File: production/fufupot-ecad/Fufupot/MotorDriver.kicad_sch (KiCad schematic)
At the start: 0 parts

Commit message: Added on to MCU outputs and added motor controller outputs
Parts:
- added 16MHz1: Crystal, 16 MHz Xtal Osc:XTAL_ABL-16_ABR, symbol Device:Crystal
- added C1, C2: 22pF, 22 pF Cap:CAP_K-SERIES_15-L2_VIS, symbol Device:C
- added C3: 10uF, 10 uF Cap:CAP_YX_5X11_RUB, symbol Device:C_Polarized
- added C5: 0.1 uF, 0.1 uF:CAP_Y5VE5TL2_VIS, symbol Device:C
- added J1: PPTC061LFBN-RC, 6 Pin:CONN6_061LFBN-RC_SUL, symbol 6 PIN Header:PPTC061LFBN-RC
- added R1: 10k, 10K Ohm:CAP_YX_5X11_RUB, symbol Device:R
- added U1: 282837-3, Screw Term 3 pin:282837-3_TYC, symbol 3 Pin Screw Term:282837-3
- added U2: ATMEGA328P-PN, footprints:28P3_ATM, symbol 2023-10-12_03-24-27:ATMEGA328P-PN
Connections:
- new net: 16MHz1.1, C2.2, U2.10 (PB7)
- new net: 16MHz1.2, C1.2, U2.9 (PB6)
- new net: C5.1, J1.1
- new net +48V: U1.3
- new net +5V: C3.1, J1.5, R1.1, U1.2, U2.20 (AVCC)
- new net CAT Heat: U2.23 (PC0)
- new net GND: C1.1, C2.1, C3.2, J1.6, U1.1, U2.7 (VCC), U2.8 (GND)
- new net PWM Speed Control: U2.15 (PB1)
- new net RESET: C5.2, R1.2, U2.1 (PC6)
- new net RX: J1.3, U2.2 (PD0)
- new net TX: J1.2, U2.3 (PD1)
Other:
- note added: "Motor Driver PCB Screw Terminal"
- note added: "This connects to the 0-5V terminal on the motor controller"

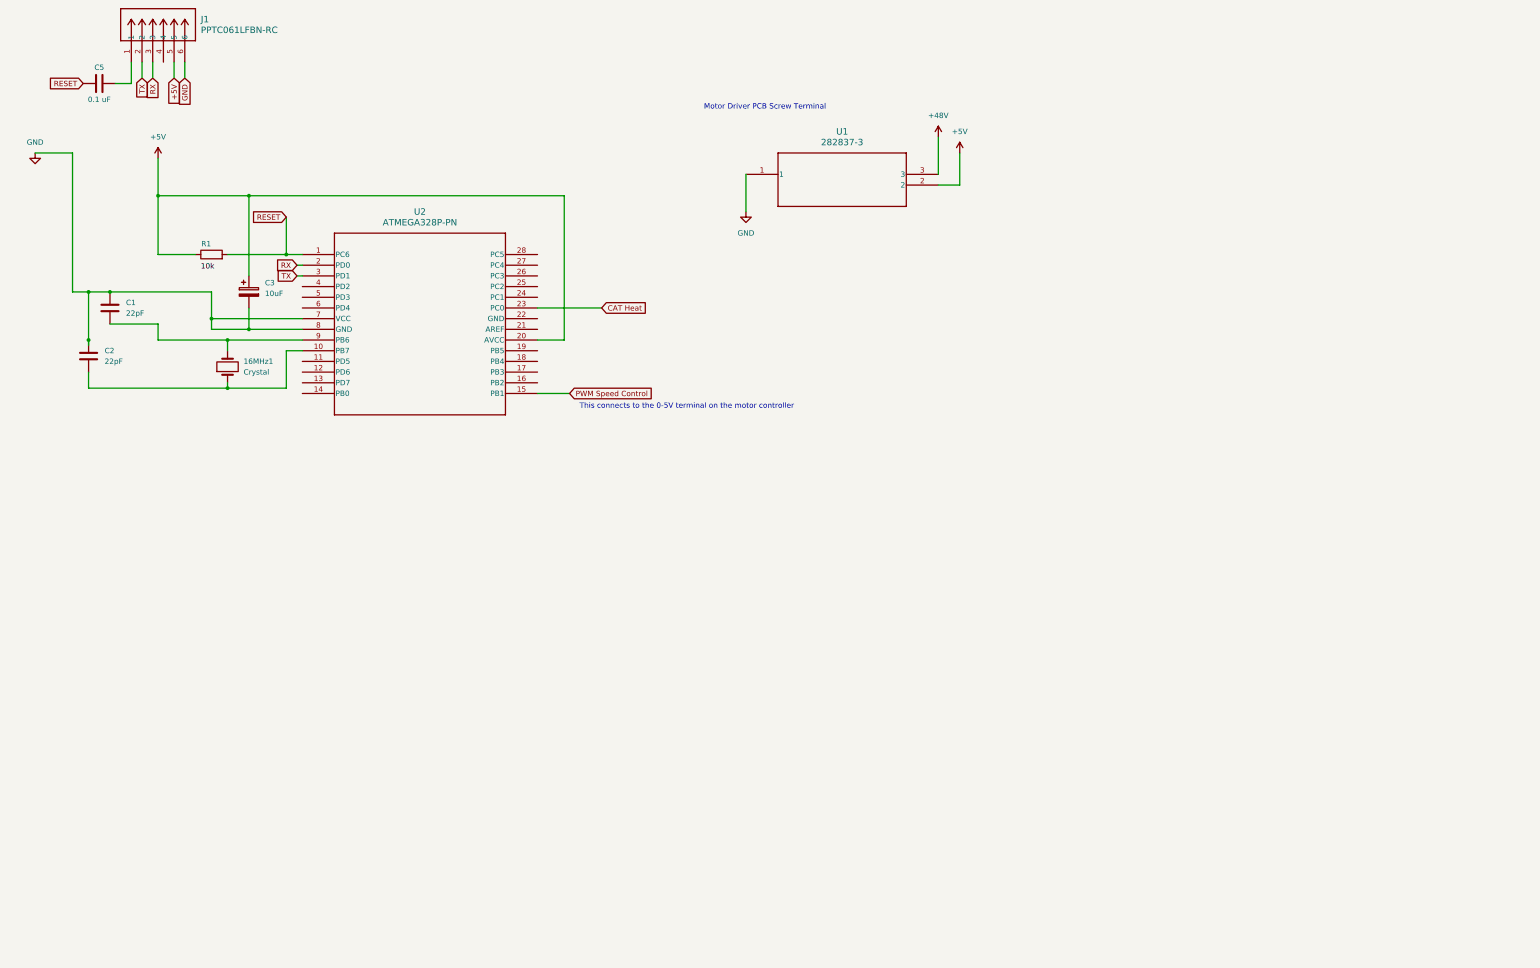
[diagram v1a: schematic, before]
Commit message: Andy's Updates
Updating from Andy's recommendation and added UART USB bridge for micro-usb code uploiad
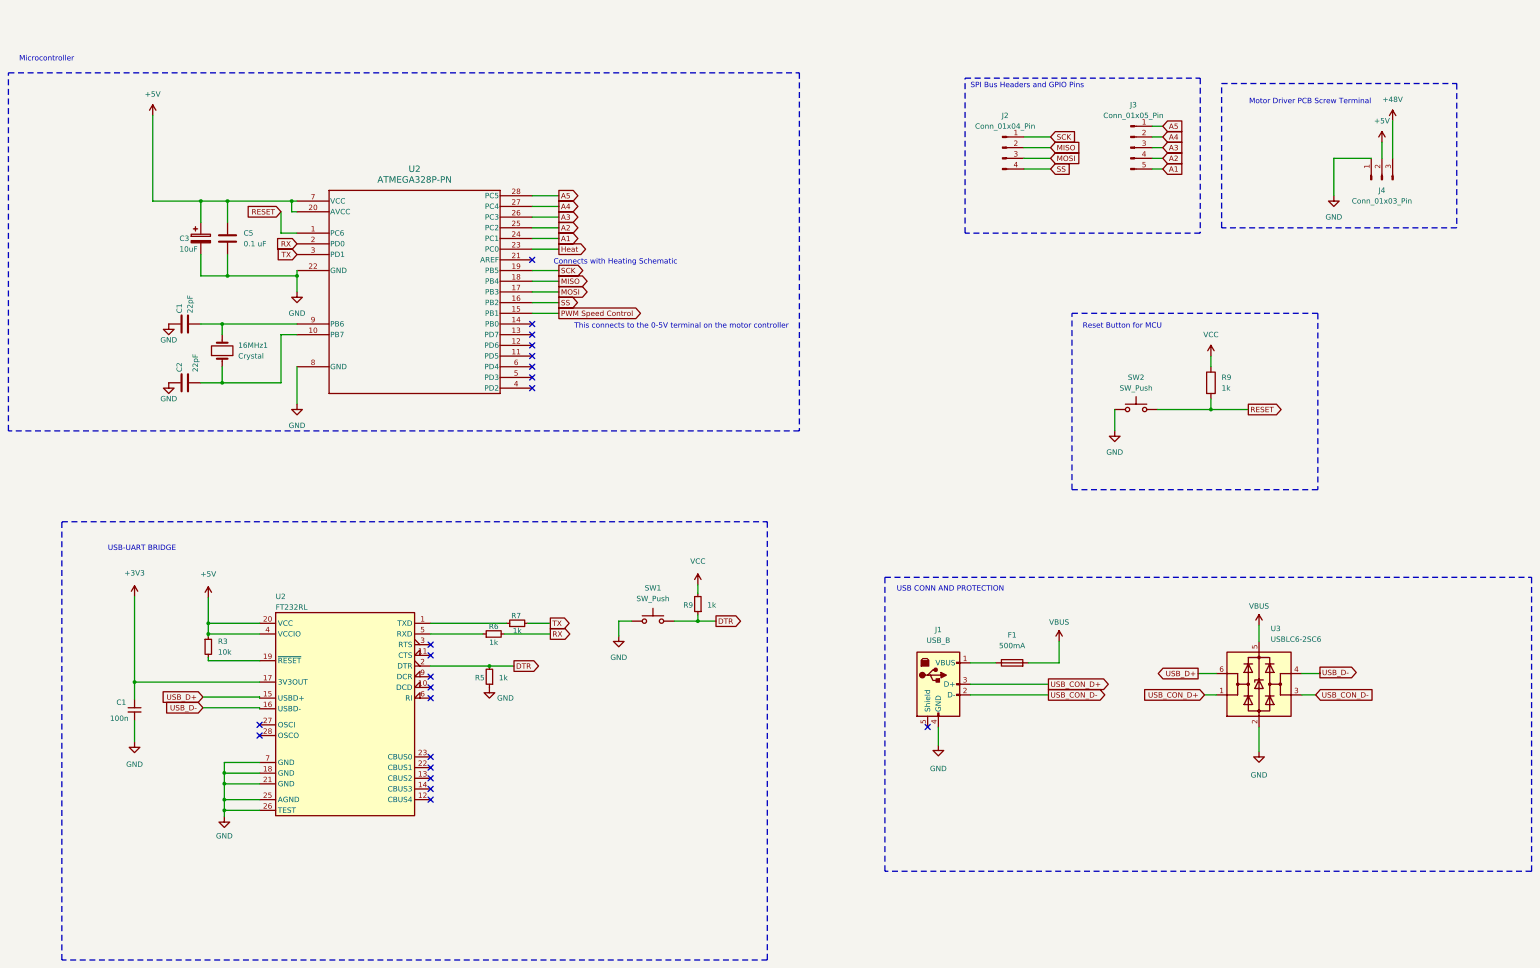
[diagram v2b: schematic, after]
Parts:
- removed J1: PPTC061LFBN-RC, 6 Pin:CONN6_061LFBN-RC_SUL, symbol 6 PIN Header:PPTC061LFBN-RC
- removed R1: 10k, 10K Ohm:CAP_YX_5X11_RUB, symbol Device:R
- removed U1: 282837-3, Screw Term 3 pin:282837-3_TYC, symbol 3 Pin Screw Term:282837-3
- added C1: 100n, Capacitor_SMD:C_0805_2012Metric, symbol Device:C_Small
- added F1: 500mA, Fuse:Fuse_1210_3225Metric, symbol Device:Fuse
- added J1: USB_B, Connector_USB:USB_Micro-B_Amphenol_10104110_Horizontal, symbol Connector:USB_B
- added J2: Conn_01x04_Pin, symbol Connector:Conn_01x04_Pin
- added J3: Conn_01x05_Pin, symbol Connector:Conn_01x05_Pin
- added J4: Conn_01x03_Pin, symbol Connector:Conn_01x03_Pin
- added R3: 10k, Resistor_SMD:R_0805_2012Metric, symbol Device:R_Small
- added R5, R6, R7, R9: 1k, Resistor_SMD:R_0805_2012Metric, symbol Device:R_Small
- added R9: 1k, symbol Device:R
- added SW1: SW_Push, Button_Switch_SMD:SW_DIP_SPSTx04_Slide_6.7x11.72mm_W6.73mm_P2.54mm_LowProfile_JPin, symbol Switch:SW_Push
- added SW2: SW_Push, symbol Switch:SW_Push
- added U2: FT232RL, Package_SO:SSOP-28_5.3x10.2mm_P0.65mm, symbol Interface_USB:FT232RL
- added U3: USBLC6-2SC6, Package_TO_SOT_SMD:SOT-23-6, symbol Power_Protection:USBLC6-2SC6
- C5: footprint 0.1 uF:CAP_Y5VE5TL2_VIS -> (none)
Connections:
- net +48V: now also J4.3 (Pin_3)
- net +5V: now also C5.1, U2.7 (VCC), J4.2 (Pin_2), R3.1, U2.20 (VCC), U2.4 (VCCIO)
- net GND: now also C5.2, U2.22 (GND), C1.2, J1.4 (GND), J4.1 (Pin_1), R5.1, SW1.1, SW2.1, U2.18 (GND), U2.21 (GND), U2.25 (AGND), U2.26 (TEST), U2.7 (GND), U3.2 (GND); no longer U2.7 (VCC)
- net RESET: now also R9.2, SW2.2; no longer C5.2
- net RX: now also R6.2
- net TX: now also R7.2
- net SS: now reaches U2.16 (PB2)
- net SS: now also J2.4 (Pin_4)
- net MOSI: now reaches U2.17 (PB3)
- net MOSI: now also J2.3 (Pin_3)
- net MISO: now reaches U2.18 (PB4)
- net MISO: now also J2.2 (Pin_2)
- net SCK: now reaches U2.19 (PB5)
- net SCK: now also J2.1 (Pin_1)
- net A1: now reaches U2.24 (PC1)
- net A1: now also J3.5 (Pin_5)
- net A2: now reaches U2.25 (PC2)
- net A2: now also J3.4 (Pin_4)
- net A3: now reaches U2.26 (PC3)
- net A3: now also J3.3 (Pin_3)
- net A4: now reaches U2.27 (PC4)
- net A4: now also J3.2 (Pin_2)
- net A5: now reaches U2.28 (PC5)
- net A5: now also J3.1 (Pin_1)
- net CAT Heat renamed Heat
- new net: R6.1, U2.5 (RXD)
- new net: F1.1, J1.1 (VBUS)
- new net: R3.2, U2.19 (~{RESET})
- new net: R7.1, U2.1 (TXD)
- new net +3V3: C1.1, U2.17 (3V3OUT)
- new net DTR: R5.2, R9.1, SW1.2, U2.2 (DTR)
- new net USB_CON_D+: J1.3 (D+), U3.1 (I/O1)
- new net USB_CON_D-: J1.2 (D-), U3.3 (I/O2)
- new net USB_D+: U2.15 (USBD+), U3.6 (I/O1)
- new net USB_D-: U2.16 (USBD-), U3.4 (I/O2)
- new net VBUS: F1.2, U3.5 (VBUS)
- new net VCC: R9.1, R9.2
- no-connect marks 0 -> 21
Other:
- note added: "Connects with Heating Schematic"
- note added: "Microcontroller"
- note added: "Reset Button for MCU"
- note added: "SPI Bus Headers and GPIO Pins"
- note added: "USB CONN AND PROTECTION"
- note added: "USB-UART BRIDGE"
- moved on the sheet: 16MHz1, C1, C2, C3, U2

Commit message: Updates unfinished
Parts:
- removed 16MHz1: Crystal, 16 MHz Xtal Osc:XTAL_ABL-16_ABR, symbol Device:Crystal
- removed C1: 100n, Capacitor_SMD:C_0805_2012Metric, symbol Device:C_Small
- removed C1, C2: 22pF, 22 pF Cap:CAP_K-SERIES_15-L2_VIS, symbol Device:C
- removed C3: 10uF, 10 uF Cap:CAP_YX_5X11_RUB, symbol Device:C_Polarized
- removed C5: 0.1 uF, symbol Device:C
- removed F1: 500mA, Fuse:Fuse_1210_3225Metric, symbol Device:Fuse
- removed J1: USB_B, Connector_USB:USB_Micro-B_Amphenol_10104110_Horizontal, symbol Connector:USB_B
- removed J2: Conn_01x04_Pin, symbol Connector:Conn_01x04_Pin
- removed J3: Conn_01x05_Pin, symbol Connector:Conn_01x05_Pin
- removed J4: Conn_01x03_Pin, symbol Connector:Conn_01x03_Pin
- removed R3: 10k, Resistor_SMD:R_0805_2012Metric, symbol Device:R_Small
- removed R5, R6, R7, R9: 1k, Resistor_SMD:R_0805_2012Metric, symbol Device:R_Small
- removed R9: 1k, symbol Device:R
- removed SW1: SW_Push, Button_Switch_SMD:SW_DIP_SPSTx04_Slide_6.7x11.72mm_W6.73mm_P2.54mm_LowProfile_JPin, symbol Switch:SW_Push
- removed SW2: SW_Push, symbol Switch:SW_Push
- removed U2: ATMEGA328P-PN, footprints:28P3_ATM, symbol 2023-10-12_03-24-27:ATMEGA328P-PN
- removed U2: FT232RL, Package_SO:SSOP-28_5.3x10.2mm_P0.65mm, symbol Interface_USB:FT232RL
- removed U3: USBLC6-2SC6, Package_TO_SOT_SMD:SOT-23-6, symbol Power_Protection:USBLC6-2SC6
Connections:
- no-connect marks 21 -> 0
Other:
- note removed: "Connects with Heating Schematic"
- note removed: "Microcontroller"
- note removed: "Motor Driver PCB Screw Terminal"
- note removed: "Reset Button for MCU"
- note removed: "SPI Bus Headers and GPIO Pins"
- note removed: "This connects to the 0-5V terminal on the motor controller"
- note removed: "USB CONN AND PROTECTION"
- note removed: "USB-UART BRIDGE"
